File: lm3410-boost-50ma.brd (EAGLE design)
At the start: 15.2 x 16.5 mm, 10 parts

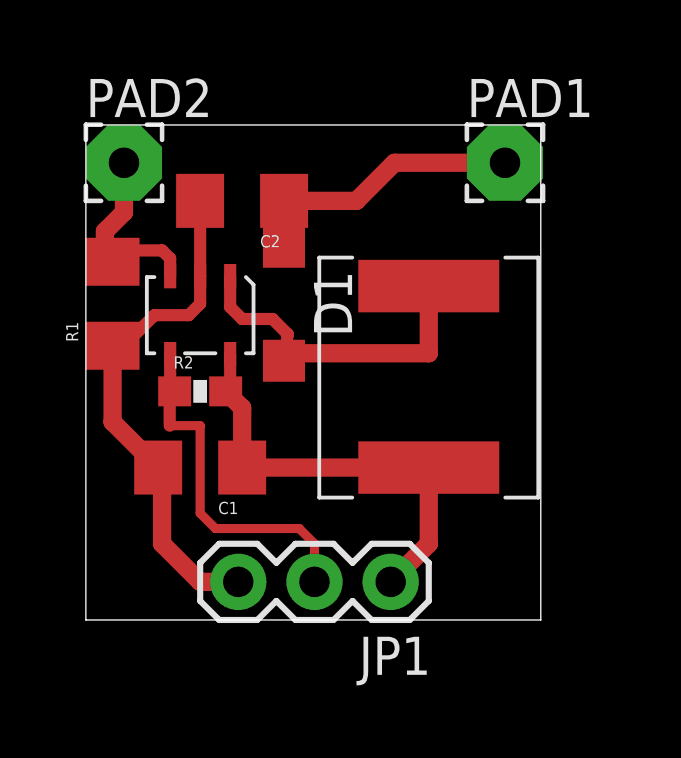
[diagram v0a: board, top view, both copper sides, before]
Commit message: Updating layout for lm3410 breakout board
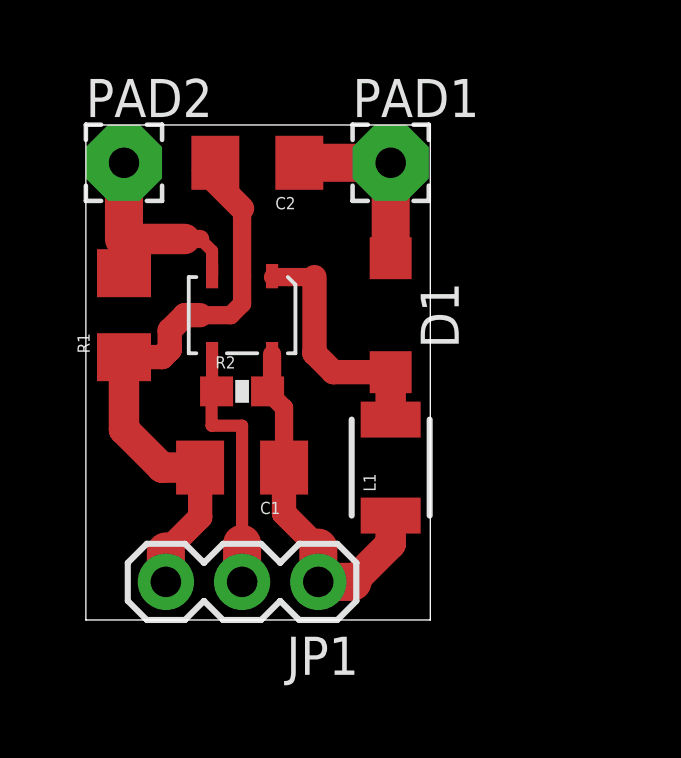
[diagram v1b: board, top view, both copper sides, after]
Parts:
- L1: value 10uF/1.2A -> 10uH/1.2A; device SparkFun-Passives:CR75 -> SparkFun-Passives:1210
- moved PAD1 3.81 mm to (10.2, 15.2)
- moved D1 3.58 mm to (10.2, 10.2)
- moved JP1 2.41 mm to (7.75, 1.27)
- moved C1 1.40 mm to (5.21, 5.08)
- moved R2 1.40 mm to (5.21, 7.62)
- moved U$1 1.40 mm to (5.21, 10.2)
- moved C2 1.37 mm to (5.71, 15.2)
- moved L1 1.27 mm to (10.2, 5.08)
- moved R1 0.54 mm to (1.27, 10.2)
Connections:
- net N$2: now also L1.2; no longer L1.P$2
- net VCC: now also L1.1; no longer L1.P$1
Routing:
- net N$10: track 10.4 -> 6.22 mm
- net DIM: track 12.2 -> 8.94 mm
- net GND: track 17.2 -> 20.2 mm
- net N$2: track 11.4 -> 8.35 mm
- net VCC: track 14.6 -> 12.2 mm
- net N$7: track 6.70 -> 7.62 mm
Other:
- board size 15.2 x 16.5 mm -> 11.5 x 16.5 mm
